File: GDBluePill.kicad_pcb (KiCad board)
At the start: 2 copper layers, 53.3 x 22.9 mm, 35 parts, among them J1 Conn_01x03, J2 Conn_01x03, J3 Conn_01x20, J4 SWD, J5 Conn_01x20, P1 USB_C_Plug_USB2.0, SW1 RESET, U1 AP1117-33, U2 STM32F103C8Tx, Y1 8MHz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

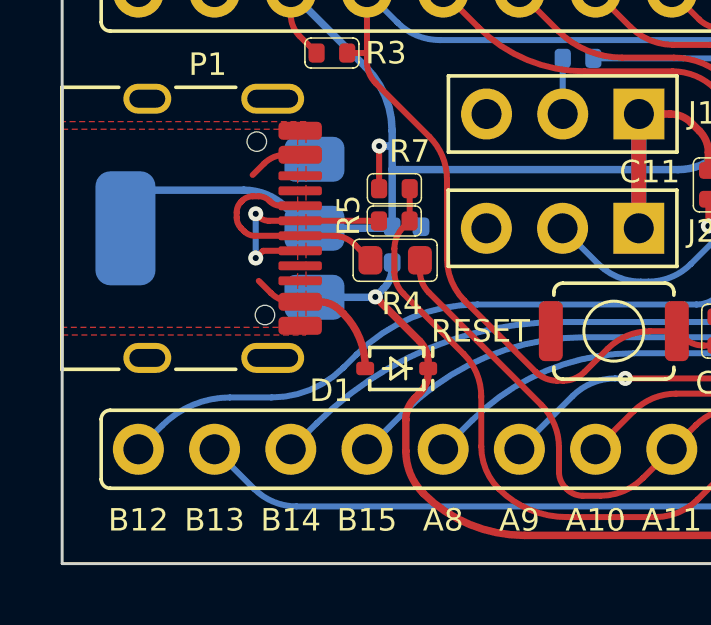
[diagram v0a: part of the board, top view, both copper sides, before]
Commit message: USB connector and pull-up resistor value fixed
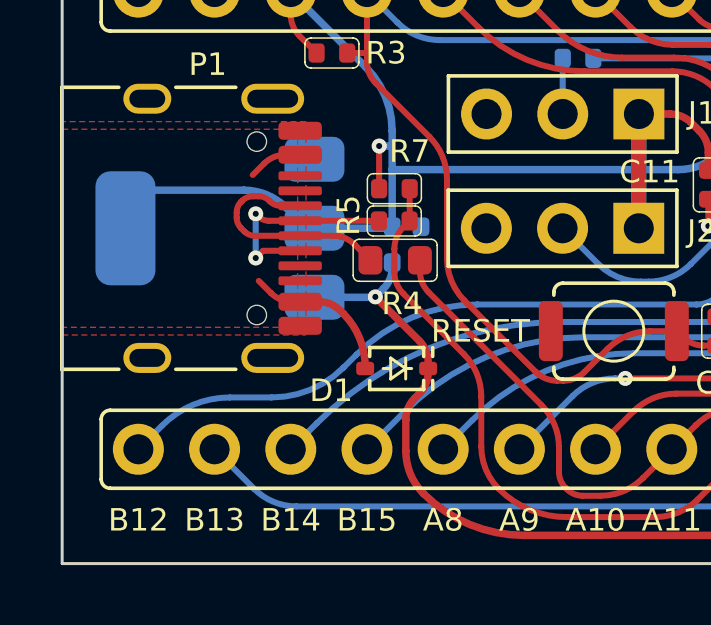
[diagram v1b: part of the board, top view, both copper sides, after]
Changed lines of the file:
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@@
     (fp_line (start -4.7 3.9) (end 4.7 3.9) (layer "F.SilkS") (width 0.12))
     (pad "" np_thru_hole circle (at -2.89 -2.6 270) (size 0.65 0.65) (drill 0.65) (layers *.Cu *.Mask))
-    (pad "" np_thru_hole circle (at 2.89 -2.8724 270) (size 0.65 0.65) (drill 0.65) (layers F&B.Cu *.Mask))
+    (pad "" np_thru_hole circle (at 2.89 -2.6 270) (size 0.65 0.65) (drill 0.65) (layers F&B.Cu *.Mask))
     (pad "A1" smd roundrect (at -3.25 -4.045 270) (size 0.6 1.45) (layers "F.Cu" "F.Paste" "F.Mask") (roundrect_rratio 0.25)
       (net 2 "GND") (pinfunction "GND") (pintype "passive"))
@@
     )
     (fp_line (start -1 -1.3) (end 1 -1.3) (layer "F.SilkS") (width 0.12))
-    (fp_line (start 1.3 -1) (end 1.3 49.2) (layer "F.SilkS") (width 0.12))
     (fp_line (start -1 49.5) (end 1 49.5) (layer "F.SilkS") (width 0.12))
     (fp_line (start -1.3 -1) (end -1.3 49.2) (layer "F.SilkS") (width 0.12))
+    (fp_line (start 1.3 -1) (end 1.3 49.2) (layer "F.SilkS") (width 0.12))
     (fp_arc (start -1 49.5) (mid -1.212132 49.412132) (end -1.3 49.2) (layer "F.SilkS") (width 0.12))
     (fp_arc (start 1.3 49.2) (mid 1.212132 49.412132) (end 1 49.5) (layer "F.SilkS") (width 0.12))
